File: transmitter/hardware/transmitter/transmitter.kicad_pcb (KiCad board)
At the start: 2 copper layers, 56 x 47 mm, 44 parts, among them J1 SOIL, J2 SOIL, J3 USB_UART, J4 PWR, J5 SOIL, J6 SOIL, J7 SOIL, J8 SOIL, Q1 Si2305CDS, Q2 BSS138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

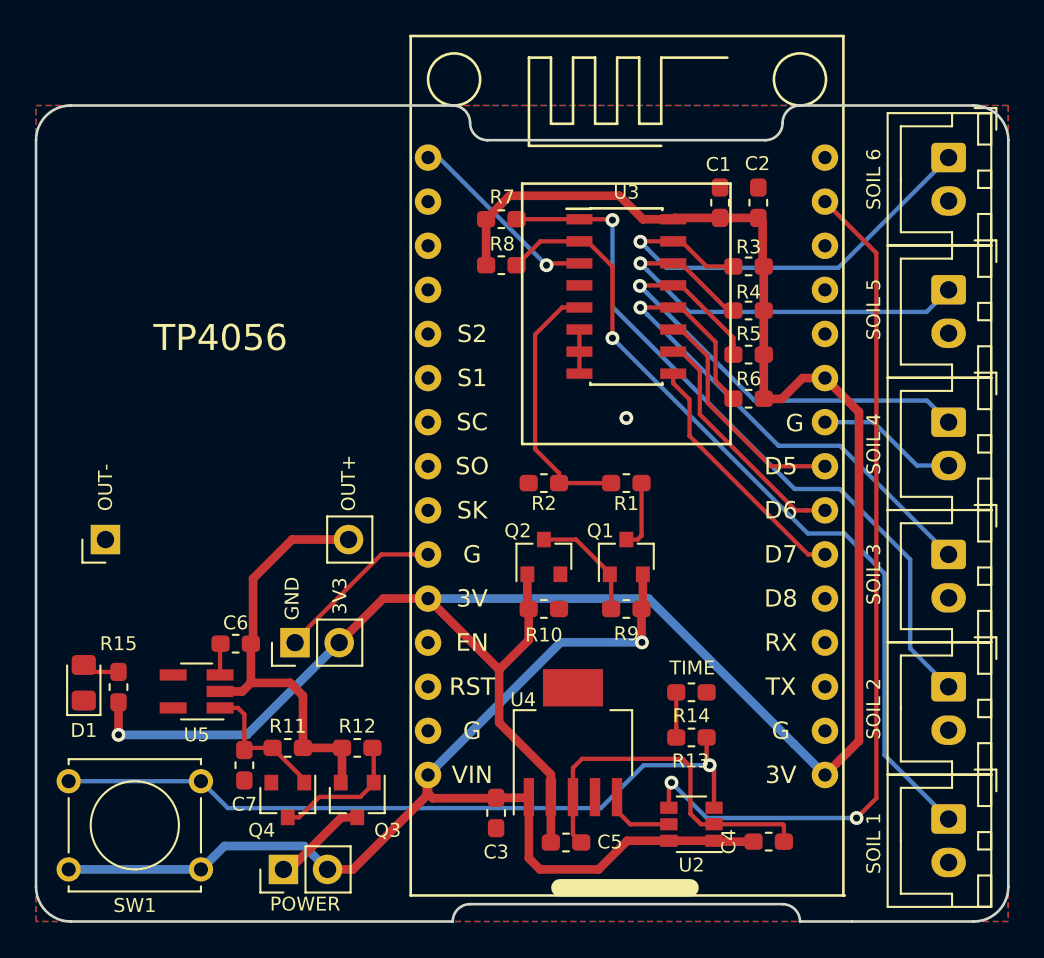
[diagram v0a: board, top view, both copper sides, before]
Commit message: Swapped sensor polarity
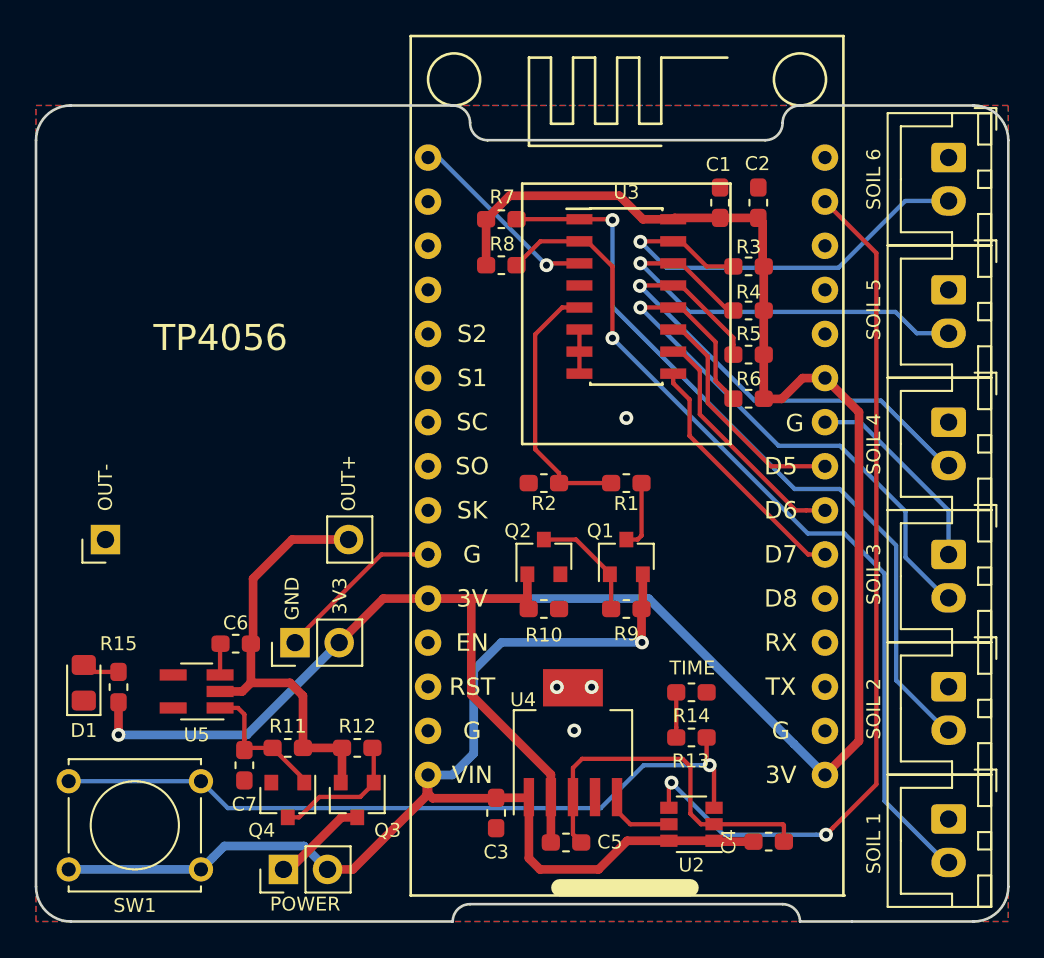
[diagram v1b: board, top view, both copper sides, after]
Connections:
- J1 pad 1: SOIL_1 -> GND
- J1 pad 2: GND -> SOIL_1
- J2 pad 1: SOIL_2 -> GND
- J2 pad 2: GND -> SOIL_2
- J5 pad 1: SOIL_3 -> GND
- J5 pad 2: GND -> SOIL_3
- J6 pad 1: SOIL_4 -> GND
- J6 pad 2: GND -> SOIL_4
- J7 pad 1: SOIL_5 -> GND
- J7 pad 2: GND -> SOIL_5
- J8 pad 1: SOIL_6 -> GND
- J8 pad 2: GND -> SOIL_6
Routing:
- net GND: track 42.8 -> 46.4 mm, vias 1 -> 4
- net /VBAT: track 68.8 -> 71.6 mm
- net SOIL_5: track 42.0 -> 44.6 mm
- net SOIL_4: track 32.5 -> 35.1 mm
- net SOIL_6: track 47.8 -> 50.4 mm
- net SOIL_3: track 28.6 -> 29.7 mm
- net SOIL_1: track 27.0 -> 25.9 mm
- net 3V3: track 132.3 -> 132.8 mm

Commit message: Graphic silkscreen
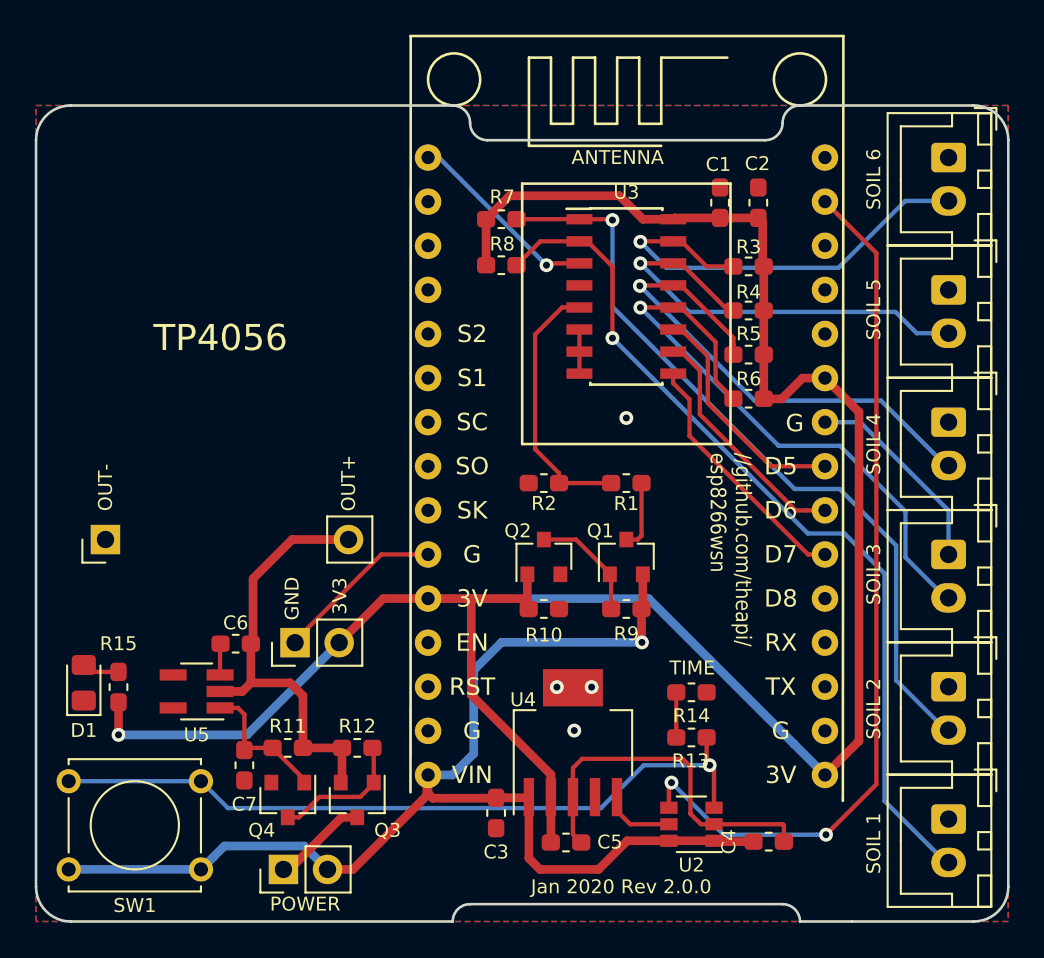
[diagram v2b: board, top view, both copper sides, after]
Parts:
- removed the REF** at (126.0, 78.2)
- added G***: LOGO, theapi:us, B.Cu at (144.6, 87.4)
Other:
- board text added: "//github.com/theapi/ esp8266wsn"
- board text added: "ANTENNA"
- board text added: "Jan 2020 Rev 2.0.0"
- board text removed: "https://github.com/theapi/esp8266wsn Jan 2020 Rev 2.0.0"

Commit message: Timer resistors on the bottom
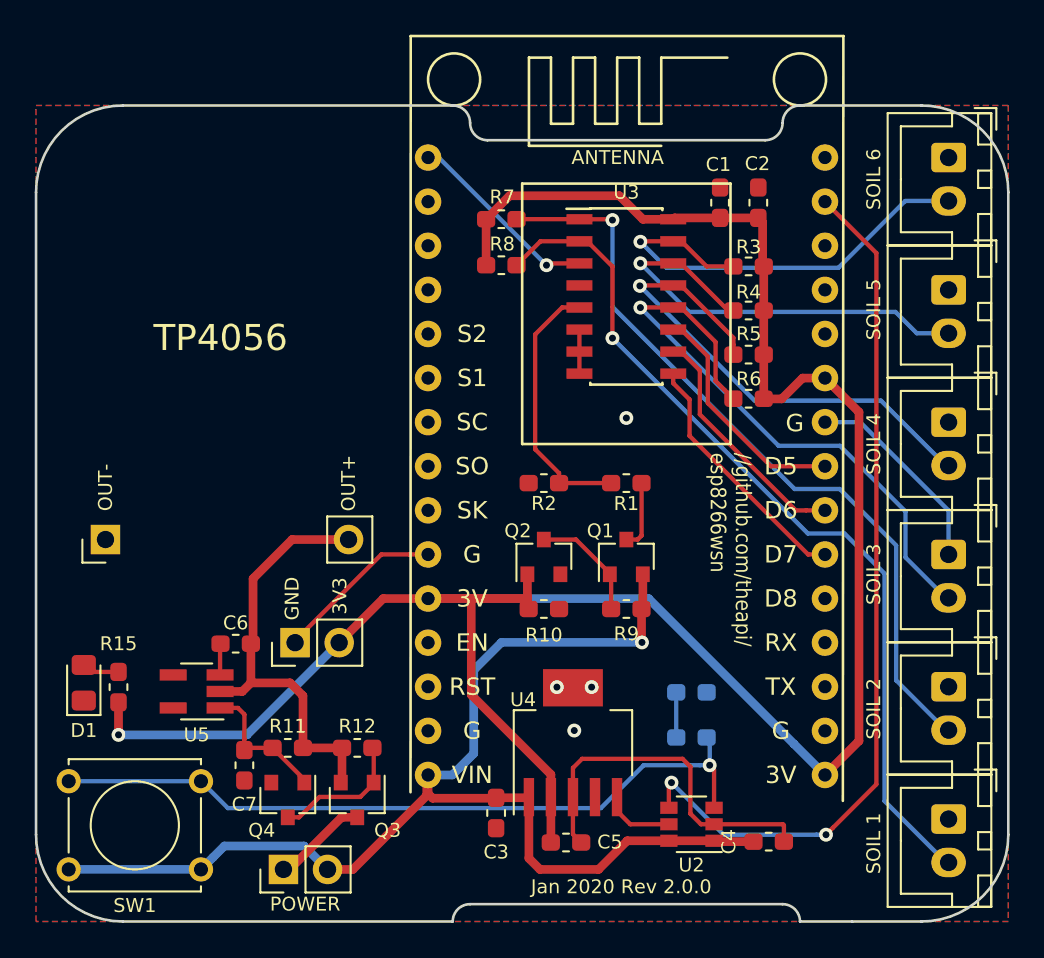
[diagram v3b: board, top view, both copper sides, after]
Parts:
- R13, R14: moved to B.Cu
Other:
- outline, holes or cut-outs redrawn
- board text removed: "TIME"

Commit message: Measure the delay time
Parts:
- added JP1: Jumper, Jumper:SolderJumper-2_P1.3mm_Open_RoundedPad1.0x1.5mm, B.Cu at (155.6, 100.0)
- added R16: 10K, Resistor_SMD:R_0603_1608Metric_Pad1.05x0.95mm_HandSolder, B.Cu at (144.1, 76.4)
- added R18: 100K, Resistor_SMD:R_0603_1608Metric_Pad1.05x0.95mm_HandSolder, B.Cu at (152.3, 98.9)
- added R19: 10K, Resistor_SMD:R_0603_1608Metric_Pad1.05x0.95mm_HandSolder, B.Cu at (148.5, 98.9)
- added TP1: TestPoint, TestPoint:TestPoint_Pad_D1.0mm, F.Cu at (134.0, 109.8)
- moved R14 4.56 mm to (148.6, 101.3), turned to 0 degrees
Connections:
- U1 pad 28: (no net) -> Net-(R16-Pad2)
- U3 pad 4: (no net) -> /DELAY_VAL
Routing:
- net /DELAY_VAL: track 0.00 -> 37.0 mm, vias 0 -> 1
- net Net-(R16-Pad2): track 0.00 -> 22.4 mm
- net Net-(TP1-Pad1): track 4.33 -> 21.2 mm, vias 0 -> 2
- net /VBAT: track 71.6 -> 76.7 mm
- net 3V3: track 132.8 -> 136.6 mm, vias 1 -> 3
- net Net-(JP1-Pad2): track 43.1 -> 45.8 mm
- net Net-(R18-Pad1): track 0.00 -> 2.05 mm
- net Net-(R13-Pad1): track 2.60 -> 2.00 mm

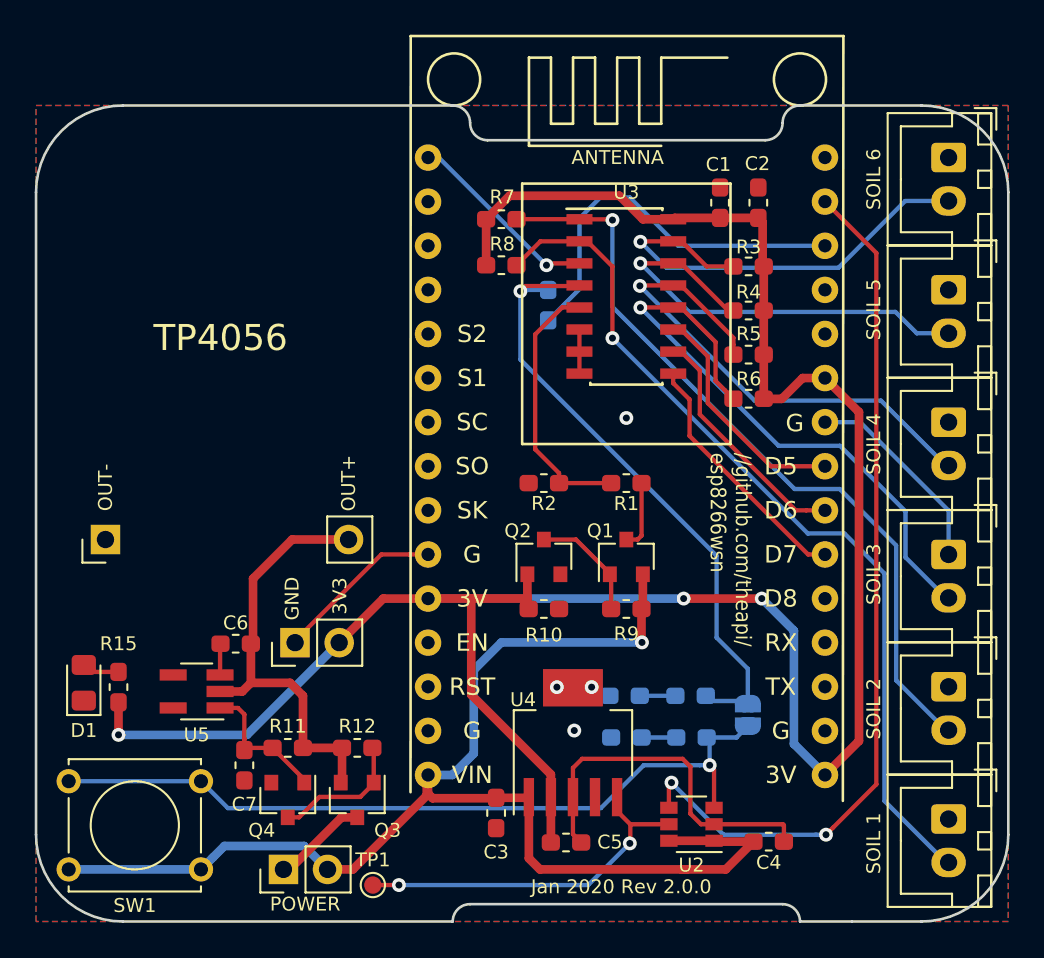
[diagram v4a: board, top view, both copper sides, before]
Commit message: Optionally measure timer resistors
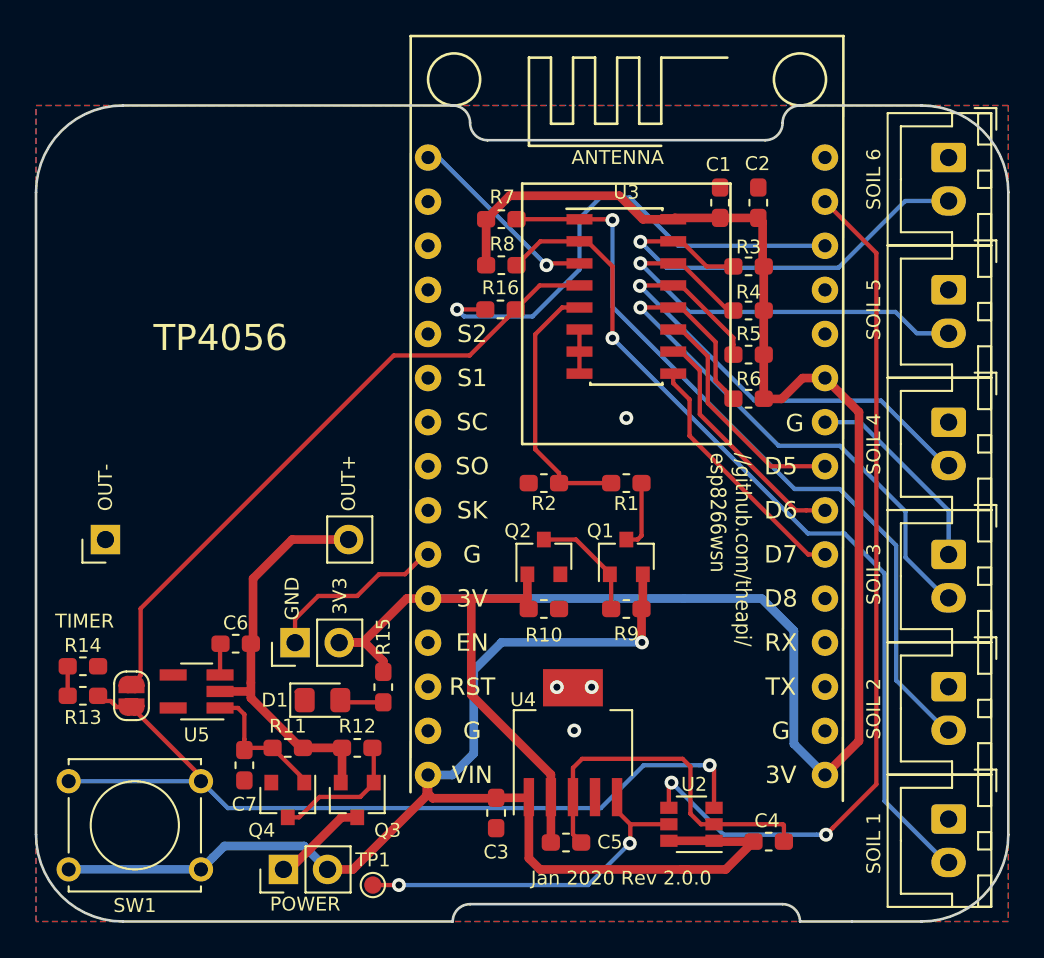
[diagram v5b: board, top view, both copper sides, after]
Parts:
- removed R18: 100K, Resistor_SMD:R_0603_1608Metric_Pad1.05x0.95mm_HandSolder
- removed R19: 10K, Resistor_SMD:R_0603_1608Metric_Pad1.05x0.95mm_HandSolder
- JP1, R13, R14, R16: moved to F.Cu
- moved JP1 35.5 mm to (120.1, 98.9)
- moved R13 35.1 mm to (117.3, 98.9)
- moved R14 31.6 mm to (117.3, 97.2), turned to 180 degrees
- moved R15 15.2 mm to (134.6, 98.4), turned to 90 degrees
- moved D1 13.8 mm to (131.1, 99.2), turned to 0 degrees
- moved R16 2.76 mm to (141.4, 76.7), turned to 180 degrees
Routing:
- net 3V3: track 136.6 -> 123.4 mm, vias 3 -> 0
- net Net-(R16-Pad2): track 22.4 -> 28.7 mm, vias 0 -> 1
- net Net-(JP1-Pad2): track 45.8 -> 49.2 mm
- net Net-(R18-Pad1): track 2.05 -> 0.00 mm
- net GND: track 46.4 -> 48.5 mm
- net /OUT+: track 25.1 -> 23.6 mm
- net /DELAY_VAL: track 37.0 -> 37.6 mm, vias 1 -> 0
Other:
- board text added: "TIMER"

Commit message: Rotated timer IC
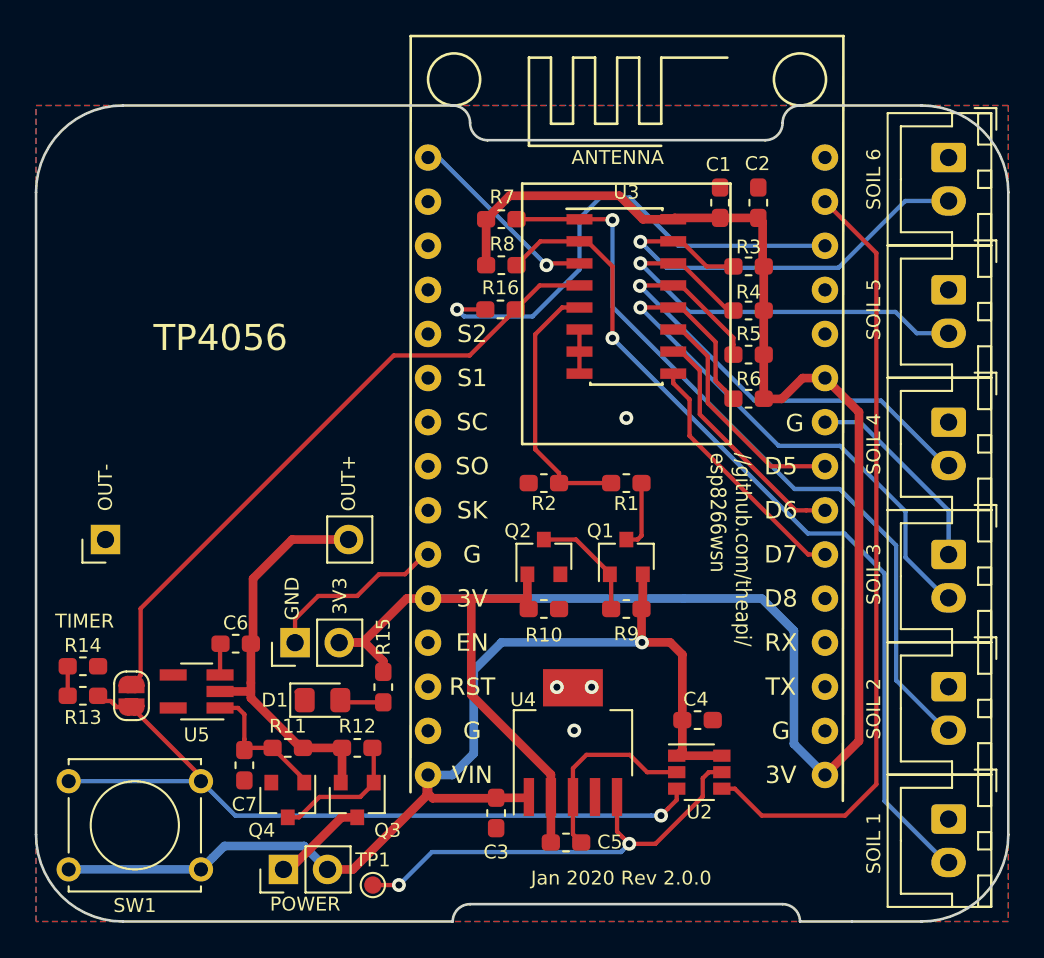
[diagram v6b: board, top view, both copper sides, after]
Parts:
- moved C4 8.11 mm to (152.7, 100.3)
- moved U2 3.03 mm to (152.8, 103.3), turned to 0 degrees
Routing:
- net /VBAT: track 76.7 -> 65.3 mm
- net GND: track 48.5 -> 38.7 mm
- net DONE: track 50.5 -> 45.1 mm, vias 2 -> 0
- net Net-(TP1-Pad1): track 21.2 -> 26.6 mm
- net Net-(JP1-Pad2): track 49.2 -> 44.6 mm
